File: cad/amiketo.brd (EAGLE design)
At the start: 69 x 35 mm, 61 parts, among them CN1 MICROSD-EJECT, J1 HEADER-5X1, Q1 IRLML6344TRPBF, Q2 DMP2035U-7, SW2 SWITCHKMR211, SW3 SWITCHKMR211, U1 STM32F411/48, U2 LIS3DH, U3 ADP5062, U5 MAX17048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

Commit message: tweak
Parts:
- moved D2 2.12 mm to (56.0, 25.5), turned to 270 degrees
- moved C12 1.50 mm to (59.0, 25.0)
- moved C16 1.50 mm to (59.0, 23.2)
- moved C1 0.50 mm to (10.5, 25.5)
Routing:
- net N$24: track 6.48 -> 3.73 mm
- net VIN: track 117.3 -> 115.7 mm
- net GND: track 145.4 -> 144.4 mm
- net VP: track 19.2 -> 20.1 mm

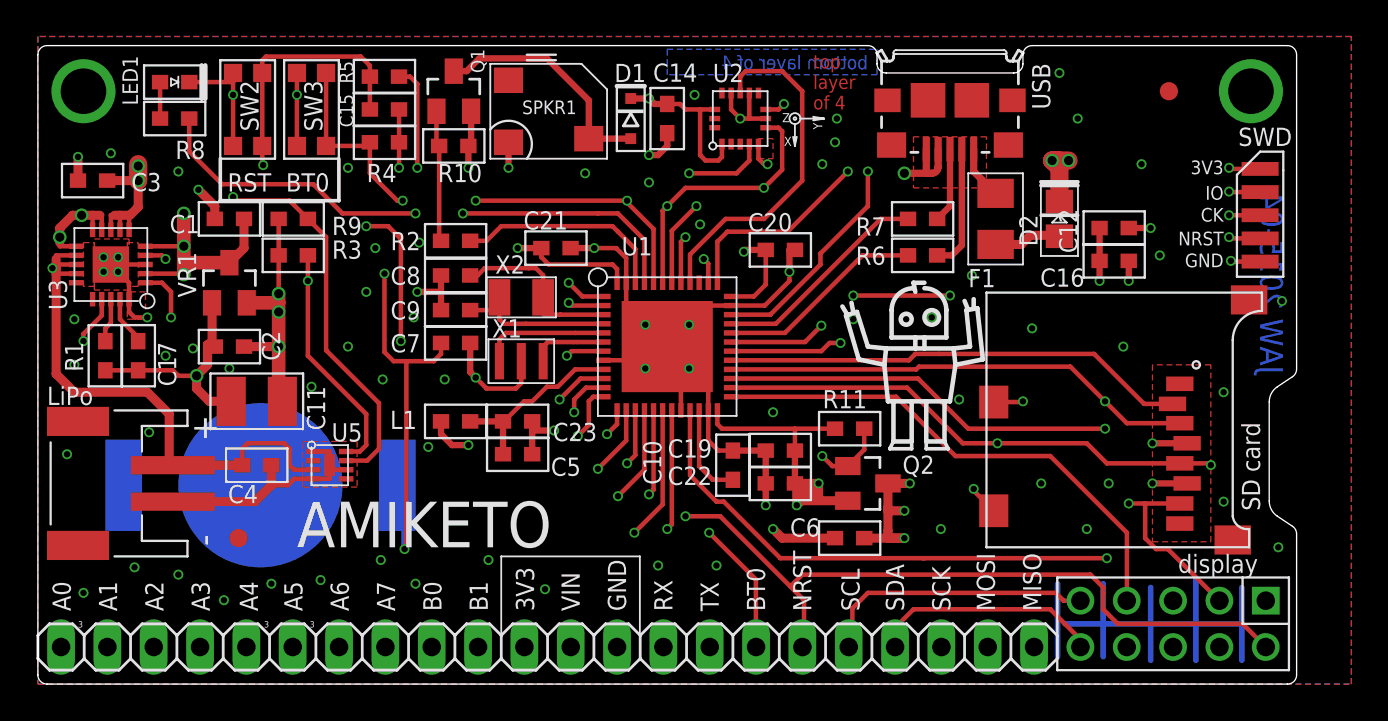
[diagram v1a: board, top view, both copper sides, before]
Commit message: display reset
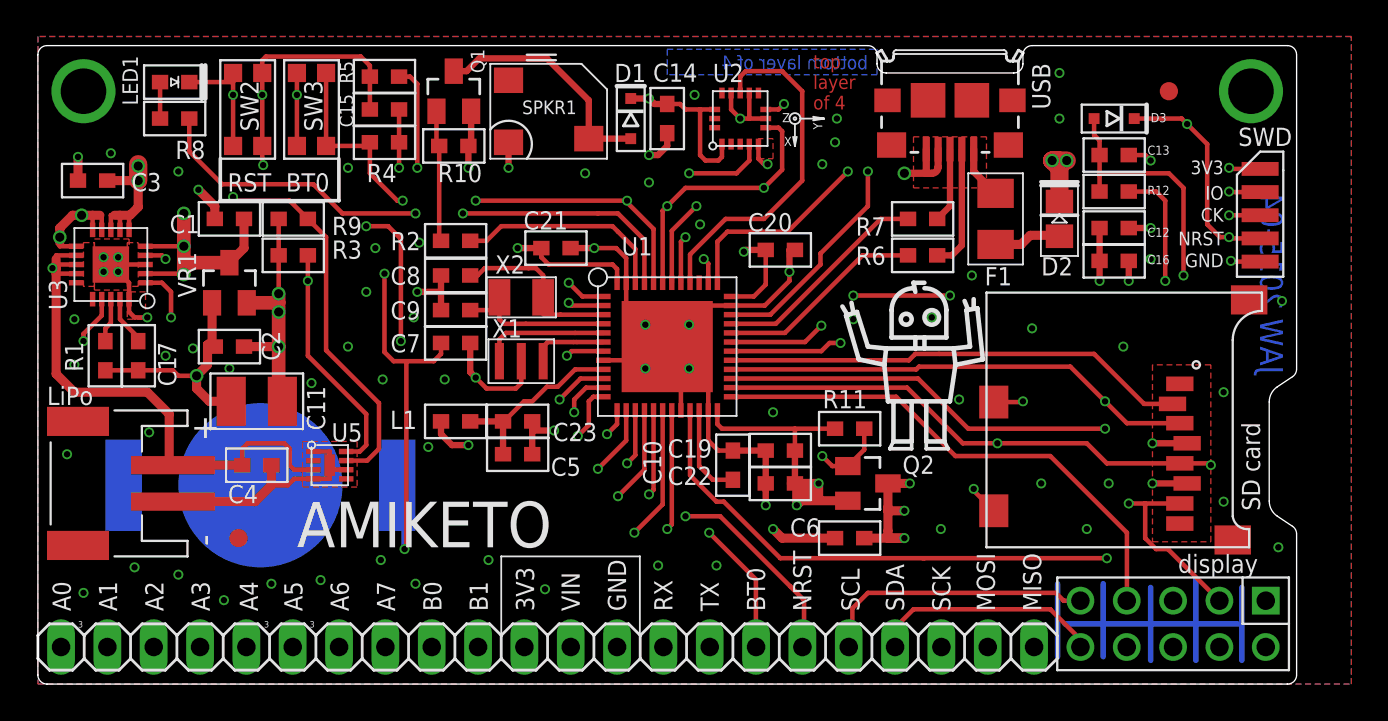
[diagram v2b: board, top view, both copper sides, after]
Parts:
- added C13: .001u, jaw:SMD0603
- added D3: any, jaw:SOD-323
- added R12: 4k7, jaw:SMD0603
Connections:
- new net NRST2: C13.1, CONN1.2, D3.A, R12.1
- net GND: now also C13.2
- net NRST: now also D3.C; no longer CONN1.2
- net VCCE: now also R12.2
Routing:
- net NRST2: track 0.00 -> 36.2 mm, vias 0 -> 1
- net NRST: track 118.4 -> 129.8 mm, vias 6 -> 8
- net VCCE: track 11.2 -> 17.8 mm, vias 5 -> 6
- net GND: track 144.4 -> 145.7 mm

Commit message: tweak
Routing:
- net VCC: track 96.8 -> 92.8 mm, vias 16 -> 17
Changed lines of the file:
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@@
 </element>
 <element name="Q2" library="jaw" package="SOT-23" value="DMP2035U-7" x="45.5" y="11" smashed="yes" rot="R270">
-<attribute name="NAME" x="47.395" y="11.5225" size="1" layer="25" font="vector" ratio="10"/>
+<attribute name="NAME" x="47.495" y="11.5225" size="1" layer="25" font="vector" ratio="10"/>
 <attribute name="VALUE" x="42.0075" y="12.905" size="1.27" layer="27" font="vector" ratio="10" rot="R270" display="off"/>
 </element>
@@
 <wire x1="37.25" y1="14.25" x2="37.5" y2="14" width="0.25" layer="1"/>
 <wire x1="37.5" y1="14" x2="41.5" y2="14" width="0.25" layer="1"/>
-<wire x1="41.5" y1="14" x2="41.5" y2="12.8" width="0.25" layer="1"/>
 <contactref element="J1" pad="P$1"/>
 <polygon width="0.35" layer="2" isolate="0.35" rank="3">
@@
 <wire x1="22.7" y1="13.1" x2="23.6" y2="13.1" width="0.35" layer="1"/>
 <contactref element="Q2" pad="2"/>
-<wire x1="41.6" y1="10.7" x2="41.6" y2="10.9" width="0.35" layer="1"/>
 <wire x1="41.6" y1="10.9" x2="41.5" y2="11" width="0.35" layer="1" curve="90"/>
 <via x="42.8" y="11" extent="1-16" drill="0.35"/>
-<wire x1="41.6" y1="9.8" x2="42.1" y2="10.9" width="0.5" layer="1"/>
-<wire x1="44.4" y1="10.05" x2="41.75" y2="10.05" width="0.5" layer="1"/>
 <contactref element="U2" pad="14"/>
 <contactref element="U2" pad="1"/>
@@
 <wire x1="40.6" y1="31.5" x2="40.9" y2="31.8" width="0.25" layer="1"/>
 <via x="65.3" y="28.3" extent="1-16" drill="0.35"/>
-<wire x1="42.8" y1="11" x2="41.6" y2="9.8" width="0.5" layer="1"/>
-<wire x1="41.6" y1="9.8" x2="41.6" y2="10.7" width="0.5" layer="1"/>
-<wire x1="42.8" y1="11" x2="41.3" y2="11" width="0.5" layer="1"/>
 <contactref element="JP1" pad="11"/>
-<wire x1="42.8" y1="11" x2="42.8" y2="10.1" width="0.5" layer="1"/>
-<wire x1="42.8" y1="10.1" x2="42.1" y2="10.8" width="0.5" layer="1"/>
 <wire x1="65.3" y1="28.3" x2="63.9" y2="29.7" width="0.35" layer="15"/>
 <wire x1="63.9" y1="29.7" x2="43.7" y2="29.7" width="0.35" layer="15"/>
@@
 <wire x1="11.45" y1="20.9" x2="13.2" y2="20.9" width="0.75" layer="1"/>
 <wire x1="13.2" y1="23.5" x2="13.2" y2="21.4" width="0.25" layer="1"/>
-<wire x1="41.6" y1="9.8" x2="41.75" y2="10.05" width="0" layer="19" extent="1-1"/>
+<via x="41.5" y="14.5" extent="1-16" drill="0.35"/>
+<wire x1="41.5" y1="14.5" x2="41.5" y2="12.8" width="0.35" layer="1"/>
+<wire x1="42.8" y1="11" x2="42.8" y2="10.05" width="0.5" layer="1"/>
+<wire x1="42.8" y1="10.05" x2="44.4" y2="10.05" width="0.5" layer="1"/>
+<wire x1="41.6" y1="9.8" x2="44.4" y2="9.8" width="0.5" layer="1"/>
+<wire x1="44.4" y1="9.8" x2="44.4" y2="10.05" width="0.5" layer="1"/>
+<wire x1="65.3" y1="28.3" x2="61" y2="25" width="0" layer="19" extent="1-1"/>
+<wire x1="40.9" y1="31.8" x2="43.7" y2="29.7" width="0" layer="19" extent="1-15"/>
+<wire x1="37.1" y1="31.5" x2="39.9" y2="31.5" width="0" layer="19" extent="1-1"/>
+<wire x1="38.8" y1="23.8" x2="37.3" y2="28.7" width="0" layer="19" extent="1-1"/>
+<wire x1="31.75" y1="22" x2="38" y2="21.25" width="0" layer="19" extent="1-1"/>
+<wire x1="25.8" y1="28.3" x2="26.3" y2="23.9" width="0" layer="19" extent="1-1"/>
+<wire x1="20.8" y1="28.3" x2="25.8" y2="28.4" width="0" layer="19" extent="1-1"/>
+<wire x1="14.2" y1="33.5" x2="19.8" y2="33.3" width="0" layer="19" extent="1-1"/>
+<wire x1="13.2" y1="25.5" x2="14.2" y2="29.5" width="0" layer="19" extent="1-1"/>
+<wire x1="13.2" y1="20.4" x2="13.2" y2="20.7" width="0" layer="19" extent="1-1"/>
+<wire x1="37.25" y1="15" x2="38" y2="21.25" width="0" layer="19" extent="1-1"/>
+<wire x1="41.5" y1="14.5" x2="41.5" y2="14" width="0" layer="19" extent="1-1"/>
+<wire x1="41.6" y1="9.8" x2="41.6" y2="10.9" width="0" layer="19" extent="1-1"/>
+<wire x1="22.1" y1="14.4" x2="13.5" y2="15.6" width="0" layer="19" extent="1-1"/>
+<wire x1="26.67" y1="2.032" x2="23.6" y2="13.1" width="0" layer="19" extent="1-1"/>
 </signal>
 <signal name="BOOT0">

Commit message: tweak
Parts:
- D1: value 200mA -> any
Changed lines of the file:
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@@
 <attribute name="VALUE" x="29.016" y="29.268" size="0.508" layer="27" rot="R90"/>
 </element>
-<element name="D1" library="jaw" package="SOD-323" value="200mA" x="32.5" y="31" smashed="yes" rot="R270">
+<element name="D1" library="jaw" package="SOD-323" value="any" x="32.5" y="31" smashed="yes" rot="R270">
 <attribute name="NAME" x="31.6" y="33" size="1" layer="25" ratio="10"/>
 <attribute name="VALUE" x="30.516" y="33.3" size="1" layer="27" ratio="10" rot="R270"/>

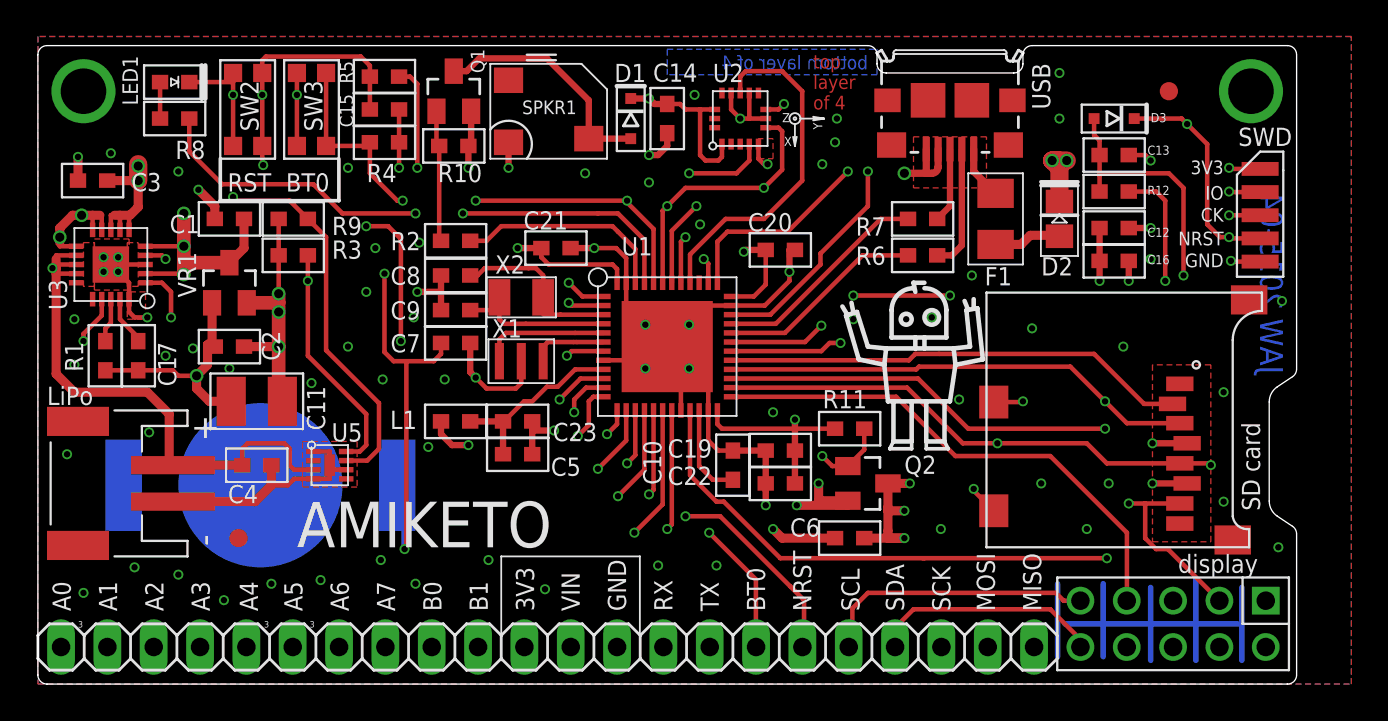
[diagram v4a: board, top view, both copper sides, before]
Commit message: tweak silk
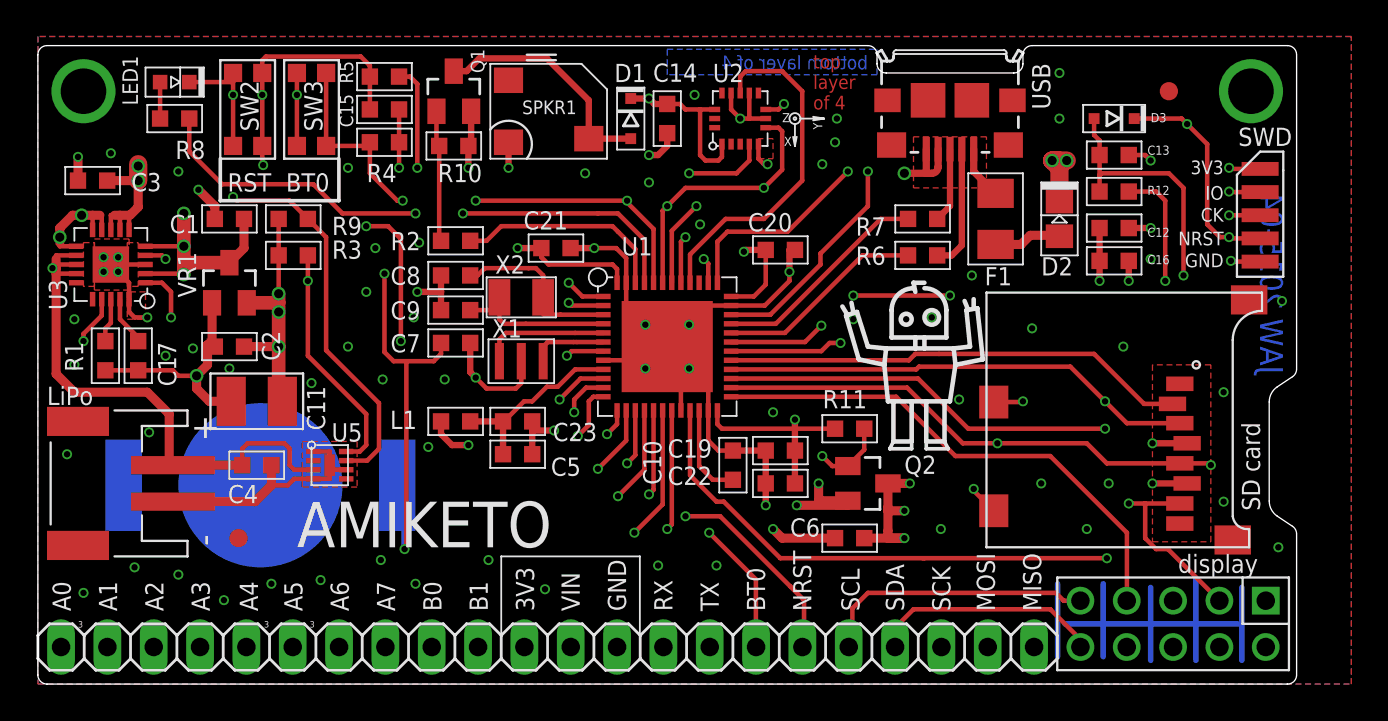
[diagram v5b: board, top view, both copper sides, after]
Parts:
- C8, C9: value 5p -> 4p7
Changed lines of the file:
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@@
 <layers>
 <layer number="1" name="Top" color="4" fill="1" visible="yes" active="yes"/>
-<layer number="2" name="V" color="5" fill="1" visible="yes" active="yes"/>
+<layer number="2" name="V" color="5" fill="1" visible="no" active="yes"/>
 <layer number="3" name="Route3" color="4" fill="3" visible="no" active="no"/>
 <layer number="14" name="Route14" color="1" fill="6" visible="no" active="no"/>
-<layer number="15" name="Signal" color="1" fill="1" visible="yes" active="yes"/>
-<layer number="16" name="Bottom" color="6" fill="1" visible="yes" active="yes"/>
+<layer number="15" name="Signal" color="1" fill="1" visible="no" active="yes"/>
+<layer number="16" name="Bottom" color="6" fill="1" visible="no" active="yes"/>
 <layer number="17" name="Pads" color="2" fill="1" visible="yes" active="yes"/>
 <layer number="18" name="Vias" color="2" fill="1" visible="yes" active="yes"/>
@@
 <layer number="20" name="Dimension" color="15" fill="1" visible="yes" active="yes"/>
 <layer number="21" name="tPlace" color="7" fill="1" visible="yes" active="yes"/>
-<layer number="22" name="bPlace" color="7" fill="1" visible="no" active="yes"/>
+<layer number="22" name="bPlace" color="7" fill="1" visible="yes" active="yes"/>
 <layer number="23" name="tOrigins" color="15" fill="1" visible="yes" active="yes"/>
 <layer number="24" name="bOrigins" color="15" fill="1" visible="yes" active="yes"/>
@@
 <wire x1="0" y1="7" x2="1.5" y2="7" width="0.1" layer="22"/>
 <wire x1="0" y1="6" x2="1.5" y2="6" width="0.1" layer="22"/>
-<text x="25.8" y="29" size="1" layer="22" ratio="10" rot="SMR180">5 mm</text>
+<text x="26" y="29" size="1" layer="22" ratio="10" rot="SMR180">5 mm</text>
 <wire x1="25" y1="30" x2="26" y2="30.2" width="0.2" layer="22"/>
 <wire x1="25.1" y1="30" x2="26" y2="29.8" width="0.2" layer="22"/>
@@
 <attribute name="VALUE" x="30.3" y="21.7" size="1" layer="27" ratio="10" rot="R180"/>
 </element>
-<element name="C8" library="jaw" package="SMD0603" value="5p" x="22.9" y="22.4" smashed="yes" rot="R180">
+<element name="C8" library="jaw" package="SMD0603" value="4p7" x="22.9" y="22.4" smashed="yes" rot="R180">
 <attribute name="NAME" x="20.978" y="22.884" size="1" layer="25" font="vector" ratio="10" rot="R180"/>
 <attribute name="VALUE" x="24.178" y="22.986" size="1" layer="27" font="vector" ratio="10" rot="R180"/>
 </element>
-<element name="C9" library="jaw" package="SMD0603" value="5p" x="22.9" y="20.5" smashed="yes" rot="R180">
+<element name="C9" library="jaw" package="SMD0603" value="4p7" x="22.9" y="20.5" smashed="yes" rot="R180">
 <attribute name="NAME" x="20.978" y="20.984" size="1" layer="25" font="vector" ratio="10" rot="R180"/>
 <attribute name="VALUE" x="24.078" y="21.086" size="1" layer="27" font="vector" ratio="10" rot="R180"/>
@@
 <element name="R12" library="jaw" package="SMD0603" value="4k7" x="59" y="27" smashed="yes">
 <attribute name="NAME" x="60.822" y="26.816" size="0.5" layer="25" font="vector" ratio="10"/>
-<attribute name="VALUE" x="57.222" y="24.914" size="1" layer="27" font="vector" ratio="10"/>
+<attribute name="VALUE" x="58.122" y="26.614" size="1" layer="27" font="vector" ratio="10"/>
 </element>
 <element name="C13" library="jaw" package="SMD0603" value=".001u" x="59" y="29" smashed="yes">
 <attribute name="NAME" x="60.822" y="29.016" size="0.5" layer="25" font="vector" ratio="10"/>
-<attribute name="VALUE" x="57.222" y="26.914" size="1" layer="27" font="vector" ratio="10"/>
+<attribute name="VALUE" x="57.622" y="28.414" size="1" layer="27" font="vector" ratio="10"/>
 </element>
 <element name="D3" library="jaw" package="SOD-323" value="any" x="59" y="31" smashed="yes" rot="R180">
